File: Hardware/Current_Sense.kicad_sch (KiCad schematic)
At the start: 32 parts, among them IC2 INA241A4IDR, IC3 AMC1350DWVR, IC4 TLV9002QDRQ1, J6 Scrut Conn, SW3 Scrut Select, U9 REF35125QDBVR

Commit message: added models
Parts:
- added TP16: 1V25, TestPoint:TestPoint_Pad_1.0x1.0mm, symbol Connector:TestPoint
- R39: footprint WSBS8518L2500JKM4 -> Parts:WSBS8518L2500JKM4
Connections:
- net +1V25: now also TP16.1
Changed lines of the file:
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@@
 	(rectangle
 		(start 134.874 27.94)
-		(end 203.2 58.42)
+		(end 213.36 58.42)
 		(stroke
 			(width 0)
@@
 	(wire
 		(pts
+			(xy 201.93 45.72) (xy 201.93 46.99)
+		)
+		(stroke
+			(width 0)
+			(type default)
+		)
+	)
+	(wire
+		(pts
 			(xy 114.3 80.01) (xy 124.46 80.01)
 		)
@@
 			)
 		)
-		(property "Footprint" "WSBS8518L2500JKM4"
+		(property "Footprint" "Parts:WSBS8518L2500JKM4"
 			(at 21.59 136.83 0)
 			(effects
@@
 	)
 	(symbol
+		(lib_id "Connector:TestPoint")
+		(at 201.93 46.99 180)
+		(unit 1)
+		(exclude_from_sim no)
+		(in_bom no)
+		(on_board yes)
+		(dnp no)
+		(fields_autoplaced yes)
+		(property "Reference" "TP16"
+			(at 204.47 49.0219 0)
+			(effects
+				(font
+					(size 1.27 1.27)
+				)
+				(justify right)
+			)
+		)
+		(property "Value" "1V25"
+			(at 204.47 51.5619 0)
+			(effects
+				(font
+					(size 1.27 1.27)
+				)
+				(justify right)
+			)
+		)
+		(property "Footprint" "TestPoint:TestPoint_Pad_1.0x1.0mm"
+			(at 196.85 46.99 0)
+			(effects
+				(font
+					(size 1.27 1.27)
+				)
+				(hide yes)
+			)
+		)
+		(property "Datasheet" "~"
+			(at 196.85 46.99 0)
+			(effects
+				(font
+					(size 1.27 1.27)
+				)
+				(hide yes)
+			)
+		)
+		(property "Description" "test point"
+			(at 201.93 46.99 0)
+			(effects
+				(font
+					(size 1.27 1.27)
+				)
+				(hide yes)
+			)
+		)
+		(pin "1"
+		)
+		(instances
+			(project "PS-AmperesPCB"
+				(path "/a452d214-ea00-440d-a445-5d6103fda43a/7e38ba4d-a54c-4f69-a074-7d0a3dae713a"
+					(reference "TP16")
+					(unit 1)
+				)
+			)
+		)
+	)
+	(symbol
 		(lib_id "Device:R_Small")
 		(at 29.21 172.72 0)
@@
 					(unit 1)
 				)
+			)
+		)
+	)
+	(symbol
+		(lib_id "power:+1V35")
+		(at 201.93 45.72 0)
+		(unit 1)
+		(exclude_from_sim no)
+		(in_bom yes)
+		(on_board yes)
+		(dnp no)
+		(fields_autoplaced yes)
+		(property "Reference" "#PWR0127"
+			(at 201.93 49.53 0)
+			(effects
+				(font
+					(size 1.27 1.27)
+				)
+				(hide yes)
+			)
+		)
+		(property "Value" "+1V25"
+			(at 201.93 40.64 0)
+			(effects
+				(font
+					(size 1.27 1.27)
+				)
+			)
+		)
+		(property "Footprint" ""
+			(at 201.93 45.72 0)
+			(effects
+				(font
+					(size 1.27 1.27)
+				)
+				(hide yes)
+			)
+		)
+		(property "Datasheet" ""
+			(at 201.93 45.72 0)
+			(effects
+				(font
+					(size 1.27 1.27)
+				)
+				(hide yes)
+			)
+		)
+		(property "Description" "Power symbol creates a global label with name \"+1V35\""
+			(at 201.93 45.72 0)
+			(effects
+				(font
+					(size 1.27 1.27)
+				)
+				(hide yes)
+			)
+		)
+		(pin "1"
+		)
+		(instances
+			(project "PS-AmperesPCB"
+				(path "/a452d214-ea00-440d-a445-5d6103fda43a/7e38ba4d-a54c-4f69-a074-7d0a3dae713a"
+					(reference "#PWR0127")
+					(unit 1)
+				)

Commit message: updated some component part nums
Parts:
- C37, C40, C42, C45, C48, C49: Mfg (none) -> MLASH168SB7104KTNA01; P/N (none) -> MLASH168SB7104KTNA01
- C38, C41, C46, C47: Mfg (none) -> MLASU168SB5105KTNA01; P/N (none) -> MLASU168SB5105KTNA01
- C39: Mfg (none) -> GRM21BR61H106KE43K
- C43: Mfg (none) -> MLASU063SB7102KFNA01; P/N (none) -> MLASU063SB7102KFNA01
- R27: Mfg (none) -> CRCW06034K30FKEA; P/N (none) -> CRCW06034K30FKEA
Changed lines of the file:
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@@
 			)
 		)
+		(property "Mfg" "MLASU063SB7102KFNA01"
+			(at 114.3 82.55 0)
+			(effects
+				(font
+					(size 1.27 1.27)
+				)
+				(hide yes)
+			)
+		)
+		(property "P/N" "MLASU063SB7102KFNA01"
+			(at 114.3 82.55 0)
+			(effects
+				(font
+					(size 1.27 1.27)
+				)
+				(hide yes)
+			)
+		)
 		(pin "2"
 		)
@@
 			)
 		)
+		(property "Mfg" "MLASH168SB7104KTNA01"
+			(at 113.03 90.17 0)
+			(effects
+				(font
+					(size 1.27 1.27)
+				)
+				(hide yes)
+			)
+		)
+		(property "P/N" "MLASH168SB7104KTNA01"
+			(at 113.03 90.17 0)
+			(effects
+				(font
+					(size 1.27 1.27)
+				)
+				(hide yes)
+			)
+		)
 		(pin "2"
 		)
@@
 			)
 		)
+		(property "Mfg" "MLASH168SB7104KTNA01"
+			(at 162.56 90.17 0)
+			(effects
+				(font
+					(size 1.27 1.27)
+				)
+				(hide yes)
+			)
+		)
+		(property "P/N" "MLASH168SB7104KTNA01"
+			(at 162.56 90.17 0)
+			(effects
+				(font
+					(size 1.27 1.27)
+				)
+				(hide yes)
+			)
+		)
 		(pin "2"
 		)
@@
 			)
 		)
+		(property "Mfg" "MLASH168SB7104KTNA01"
+			(at 69.85 81.28 0)
+			(effects
+				(font
+					(size 1.27 1.27)
+				)
+				(hide yes)
+			)
+		)
+		(property "P/N" "MLASH168SB7104KTNA01"
+			(at 69.85 81.28 0)
+			(effects
+				(font
+					(size 1.27 1.27)
+				)
+				(hide yes)
+			)
+		)
 		(pin "2"
 		)
@@
 			)
 		)
+		(property "Mfg" "MLASH168SB7104KTNA01"
+			(at 144.78 48.26 0)
+			(effects
+				(font
+					(size 1.27 1.27)
+				)
+				(hide yes)
+			)
+		)
+		(property "P/N" "MLASH168SB7104KTNA01"
+			(at 144.78 48.26 0)
+			(effects
+				(font
+					(size 1.27 1.27)
+				)
+				(hide yes)
+			)
+		)
 		(pin "2"
 		)
@@
 			)
 		)
+		(property "Mfg" "CRCW06034K30FKEA"
+			(at 208.28 83.82 90)
+			(effects
+				(font
+					(size 1.27 1.27)
+				)
+				(hide yes)
+			)
+		)
+		(property "P/N" "CRCW06034K30FKEA"
+			(at 208.28 83.82 90)
+			(effects
+				(font
+					(size 1.27 1.27)
+				)
+				(hide yes)
+			)
+		)
 		(pin "2"
 		)
@@
 			)
 		)
+		(property "Mfg" "MLASU168SB5105KTNA01"
+			(at 121.92 90.17 0)
+			(effects
+				(font
+					(size 1.27 1.27)
+				)
+				(hide yes)
+			)
+		)
+		(property "P/N" "MLASU168SB5105KTNA01"
+			(at 121.92 90.17 0)
+			(effects
+				(font
+					(size 1.27 1.27)
+				)
+				(hide yes)
+			)
+		)
 		(pin "2"
 		)
@@
 			)
 		)
+		(property "Mfg" "GRM21BR61H106KE43K"
+			(at 175.26 49.53 0)
+			(effects
+				(font
+					(size 1.27 1.27)
+				)
+				(hide yes)
+			)
+		)
 		(pin "2"
 		)
@@
 			)
 		)
+		(property "Mfg" "MLASU168SB5105KTNA01"
+			(at 153.67 48.26 0)
+			(effects
+				(font
+					(size 1.27 1.27)
+				)
+				(hide yes)
+			)
+		)
+		(property "P/N" "MLASU168SB5105KTNA01"
+			(at 153.67 48.26 0)
+			(effects
+				(font
+					(size 1.27 1.27)
+				)
+				(hide yes)
+			)
+		)
 		(pin "2"
 		)
@@
 			)
 		)
+		(property "Mfg" "MLASU168SB5105KTNA01"
+			(at 212.09 74.93 0)
+			(effects
+				(font
+					(size 1.27 1.27)
+				)
+				(hide yes)
+			)
+		)
+		(property "P/N" "MLASU168SB5105KTNA01"
+			(at 212.09 74.93 0)
+			(effects
+				(font
+					(size 1.27 1.27)
+				)
+				(hide yes)
+			)
+		)
 		(pin "2"
 		)
@@
 			)
 		)
+		(property "Mfg" "MLASH168SB7104KTNA01"
+			(at 185.42 49.53 0)
+			(effects
+				(font
+					(size 1.27 1.27)
+				)
+				(hide yes)
+			)
+		)
+		(property "P/N" "MLASH168SB7104KTNA01"
+			(at 185.42 49.53 0)
+			(effects
+				(font
+					(size 1.27 1.27)
+				)
+				(hide yes)
+			)
+		)
 		(pin "2"
 		)
@@
 			)
 		)
+		(property "Mfg" "MLASH168SB7104KTNA01"
+			(at 251.46 105.41 0)
+			(effects
+				(font
+					(size 1.27 1.27)
+				)
+				(hide yes)
+			)
+		)
+		(property "P/N" "MLASH168SB7104KTNA01"
+			(at 251.46 105.41 0)
+			(effects
+				(font
+					(size 1.27 1.27)
+				)
+				(hide yes)
+			)
+		)
 		(pin "2"
 		)
@@
 			(at 154.94 90.17 0)
 			(effects
+				(font
+					(size 1.27 1.27)
+				)
+				(hide yes)
+			)
+		)
+		(property "Mfg" "MLASU168SB5105KTNA01"
+			(at 154.94 90.17 0)
+			(effects
+				(font
+					(size 1.27 1.27)
+				)
+				(hide yes)
+			)
+		)
+		(property "P/N" "MLASU168SB5105KTNA01"
+			(at 154.94 90.17 0)
+			(effects

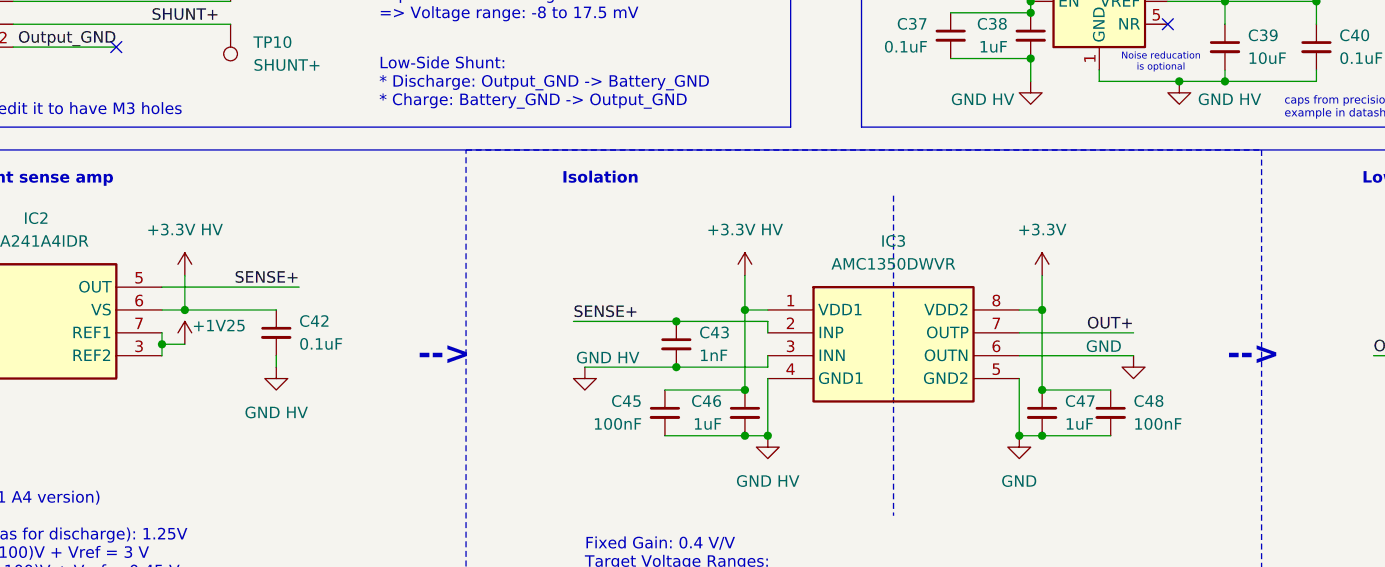
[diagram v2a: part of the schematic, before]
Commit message: new dpdt switch, layout done
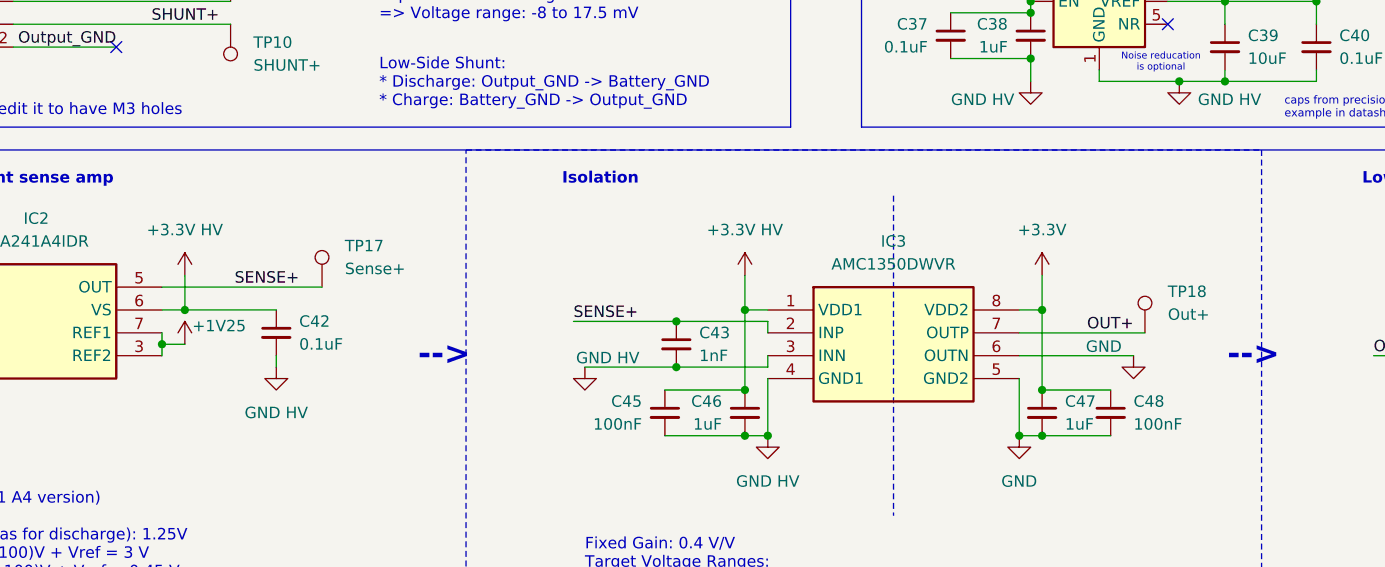
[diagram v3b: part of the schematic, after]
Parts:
- added TP17: Sense+, TestPoint:TestPoint_Keystone_5005-5009_Compact, symbol Connector:TestPoint
- added TP18: Out+, TestPoint:TestPoint_Keystone_5005-5009_Compact, symbol Connector:TestPoint
- J6: P/N (none) -> 105309-1202
- SW3: footprint Button_Switch_SMD:SW_DPDT_CK_JS202011JCQN -> Parts:CAS220TB
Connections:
- net OUT+: now also TP18.1
- net SENSE+: now also TP17.1
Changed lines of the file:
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@@
 	(wire
 		(pts
-			(xy 57.15 76.2) (xy 72.39 76.2)
+			(xy 57.15 76.2) (xy 74.93 76.2)
 		)
 		(stroke
@@
 	(wire
 		(pts
-			(xy 152.4 81.28) (xy 165.1 81.28)
+			(xy 152.4 81.28) (xy 166.37 81.28)
 		)
 		(stroke
@@
 	)
 	(symbol
+		(lib_id "Connector:TestPoint")
+		(at 166.37 81.28 0)
+		(unit 1)
+		(exclude_from_sim no)
+		(in_bom yes)
+		(on_board yes)
+		(dnp no)
+		(fields_autoplaced yes)
+		(property "Reference" "TP18"
+			(at 168.91 76.7079 0)
+			(effects
+				(font
+					(size 1.27 1.27)
+				)
+				(justify left)
+			)
+		)
+		(property "Value" "Out+"
+			(at 168.91 79.2479 0)
+			(effects
+				(font
+					(size 1.27 1.27)
+				)
+				(justify left)
+			)
+		)
+		(property "Footprint" "TestPoint:TestPoint_Keystone_5005-5009_Compact"
+			(at 171.45 81.28 0)
+			(effects
+				(font
+					(size 1.27 1.27)
+				)
+				(hide yes)
+			)
+		)
+		(property "Datasheet" "~"
+			(at 171.45 81.28 0)
+			(effects
+				(font
+					(size 1.27 1.27)
+				)
+				(hide yes)
+			)
+		)
+		(property "Description" "test point"
+			(at 166.37 81.28 0)
+			(effects
+				(font
+					(size 1.27 1.27)
+				)
+				(hide yes)
+			)
+		)
+		(pin "1"
+		)
+		(instances
+			(project ""
+				(path "/a452d214-ea00-440d-a445-5d6103fda43a/7e38ba4d-a54c-4f69-a074-7d0a3dae713a"
+					(reference "TP18")
+					(unit 1)
+				)
+			)
+		)
+	)
+	(symbol
 		(lib_id "Device:D_Zener")
 		(at 262.89 87.63 270)
@@
 			)
 		)
+		(property "P/N" "105309-1202"
+			(at 76.2 176.53 0)
+			(effects
+				(font
+					(size 1.27 1.27)
+				)
+				(hide yes)
+			)
+		)
 		(pin "2"
 		)
@@
 			)
 		)
-		(property "Footprint" "Button_Switch_SMD:SW_DPDT_CK_JS202011JCQN"
+		(property "Footprint" "Parts:CAS220TB"
 			(at 74.93 167.64 0)
 			(effects
@@
 			)
 		)
-		(property "Footprint" "Button_Switch_SMD:SW_DPDT_CK_JS202011JCQN"
+		(property "Footprint" "Parts:CAS220TB"
 			(at 74.93 152.4 0)
 			(effects
@@
 					(unit 1)
 				)
+			)
+		)
+	)
+	(symbol
+		(lib_id "Connector:TestPoint")
+		(at 74.93 76.2 0)
+		(unit 1)
+		(exclude_from_sim no)
+		(in_bom yes)
+		(on_board yes)
+		(dnp no)
+		(fields_autoplaced yes)
+		(property "Reference" "TP17"
+			(at 77.47 71.6279 0)
+			(effects
+				(font
+					(size 1.27 1.27)
+				)
+				(justify left)
+			)
+		)
+		(property "Value" "Sense+"
+			(at 77.47 74.1679 0)
+			(effects
+				(font
+					(size 1.27 1.27)
+				)
+				(justify left)
+			)
+		)
+		(property "Footprint" "TestPoint:TestPoint_Keystone_5005-5009_Compact"
+			(at 80.01 76.2 0)
+			(effects
+				(font
+					(size 1.27 1.27)
+				)
+				(hide yes)
+			)
+		)
+		(property "Datasheet" "~"
+			(at 80.01 76.2 0)
+			(effects
+				(font
+					(size 1.27 1.27)
+				)
+				(hide yes)
+			)
+		)
+		(property "Description" "test point"
+			(at 74.93 76.2 0)
+			(effects
+				(font
+					(size 1.27 1.27)
+				)
+				(hide yes)
+			)
+		)
+		(pin "1"
+		)
+		(instances
+			(project ""
+				(path "/a452d214-ea00-440d-a445-5d6103fda43a/7e38ba4d-a54c-4f69-a074-7d0a3dae713a"
+					(reference "TP17")
+					(unit 1)
+				)

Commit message: generated production stuff
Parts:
- IC2: P/N (none) -> INA241A4IDR
- IC3: P/N (none) -> AMC1350DWVR
- IC4: P/N (none) -> TLV9002QDRQ1
- R25: Mfg (none) -> 0603WAF8201T5E; P/N (none) -> 0603WAF8201T5E
- R26: Mfg (none) -> 0603WAJ0332T5E; P/N (none) -> 0603WAJ0332T5E
- R28: Mfg (none) -> 0603WAF3402T5E; P/N (none) -> 0603WAF3402T5E
- R29: Mfg (none) -> 0603WAF510JT5E; P/N (none) -> 0603WAF510JT5E
- R39: Manufacturer_Part_Number WSBS8518L2500JTP3 -> (none); Mfg (none) -> WSBS8518L2500JTP3; P/N (none) -> WSBS8518L2500JTP3
- SW3: Mfg (none) -> CAS-220TB; P/N (none) -> CAS-220TB
- U9: P/N (none) -> REF35125QDBVR
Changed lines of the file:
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@@
 			)
 		)
-		(property "Manufacturer_Part_Number" "WSBS8518L2500JTP3"
+		(property "P/N" "WSBS8518L2500JTP3"
 			(at 21.59 836.83 0)
 			(effects
@@
 			)
 		)
+		(property "Mfg" "WSBS8518L2500JTP3"
+			(at 40.64 41.91 0)
+			(effects
+				(font
+					(size 1.27 1.27)
+				)
+				(hide yes)
+			)
+		)
 		(pin "1"
 		)
@@
 			)
 		)
+		(property "Mfg" "0603WAF510JT5E"
+			(at 29.21 172.72 0)
+			(effects
+				(font
+					(size 1.27 1.27)
+				)
+				(hide yes)
+			)
+		)
+		(property "P/N" "0603WAF510JT5E"
+			(at 29.21 172.72 0)
+			(effects
+				(font
+					(size 1.27 1.27)
+				)
+				(hide yes)
+			)
+		)
 		(pin "1"
 		)
@@
 			)
 		)
+		(property "P/N" "INA241A4IDR"
+			(at 29.21 76.2 0)
+			(effects
+				(font
+					(size 1.27 1.27)
+				)
+				(hide yes)
+			)
+		)
 		(pin "8"
 		)
@@
 			)
 		)
+		(property "P/N" "TLV9002QDRQ1"
+			(at 218.44 81.28 0)
+			(effects
+				(font
+					(size 1.27 1.27)
+				)
+				(hide yes)
+			)
+		)
 		(pin "1"
 		)
@@
 			)
 		)
+		(property "P/N" "REF35125QDBVR"
+			(at 161.29 44.45 0)
+			(effects
+				(font
+					(size 1.27 1.27)
+				)
+				(hide yes)
+			)
+		)
 		(pin "2"
 		)
@@
 			)
 		)
+		(property "Mfg" "0603WAJ0332T5E"
+			(at 200.66 83.82 90)
+			(effects
+				(font
+					(size 1.27 1.27)
+				)
+				(hide yes)
+			)
+		)
+		(property "P/N" "0603WAJ0332T5E"
+			(at 200.66 83.82 90)
+			(effects
+				(font
+					(size 1.27 1.27)
+				)
+				(hide yes)
+			)
+		)
 		(pin "2"
 		)
@@
 			)
 		)
+		(property "Mfg" "0603WAF3402T5E"
+			(at 29.21 160.02 0)
+			(effects
+				(font
+					(size 1.27 1.27)
+				)
+				(hide yes)
+			)
+		)
+		(property "P/N" "0603WAF3402T5E"
+			(at 29.21 160.02 0)
+			(effects
+				(font
+					(size 1.27 1.27)
+				)
+				(hide yes)
+			)
+		)
 		(pin "1"
 		)
@@
 			)
 		)
-		(property "Datasheet" "~"
+		(property "Datasheet" "https://www.nidec-components.com/e/catalog/switch/cas.pdf"
 			(at 74.93 167.64 0)
 			(effects
@@
 			)
 		)
+		(property "P/N" "CAS-220TB"
+			(at 74.93 167.64 0)
+			(effects
+				(font
+					(size 1.27 1.27)
+				)
+				(hide yes)
+			)
+		)
+		(property "Mfg" "CAS-220TB"
+			(at 74.93 167.64 0)
+			(effects
+				(font
+					(size 1.27 1.27)
+				)
+				(hide yes)
+			)
+		)
 		(pin "5"
 		)
@@
 			)
 		)
+		(property "P/N" "AMC1350DWVR"
+			(at 124.46 78.74 0)
+			(effects
+				(font
+					(size 1.27 1.27)
+				)
+				(hide yes)
+			)
+		)
 		(pin "6"
 		)
@@
 			)
 		)
-		(property "Datasheet" "~"
+		(property "Datasheet" "https://www.nidec-components.com/e/catalog/switch/cas.pdf"
 			(at 74.93 152.4 0)
 			(effects
@@
 			)
 		)
+		(property "P/N" "CAS-220TB"
+			(at 74.93 152.4 0)
+			(effects
+				(font
+					(size 1.27 1.27)
+				)
+				(hide yes)
+			)
+		)
+		(property "Mfg" "CAS-220TB"
+			(at 74.93 152.4 0)
+			(effects
+				(font
+					(size 1.27 1.27)
+				)
+				(hide yes)
+			)
+		)
 		(pin "5"
 		)
@@
 			(at 204.47 74.93 0)
 			(effects
+				(font
+					(size 1.27 1.27)
+				)
+				(hide yes)
+			)
+		)
+		(property "Mfg" "0603WAF8201T5E"
+			(at 204.47 74.93 0)
+			(effects
+				(font
+					(size 1.27 1.27)
+				)
+				(hide yes)
+			)
+		)
+		(property "P/N" "0603WAF8201T5E"
+			(at 204.47 74.93 0)
+			(effects

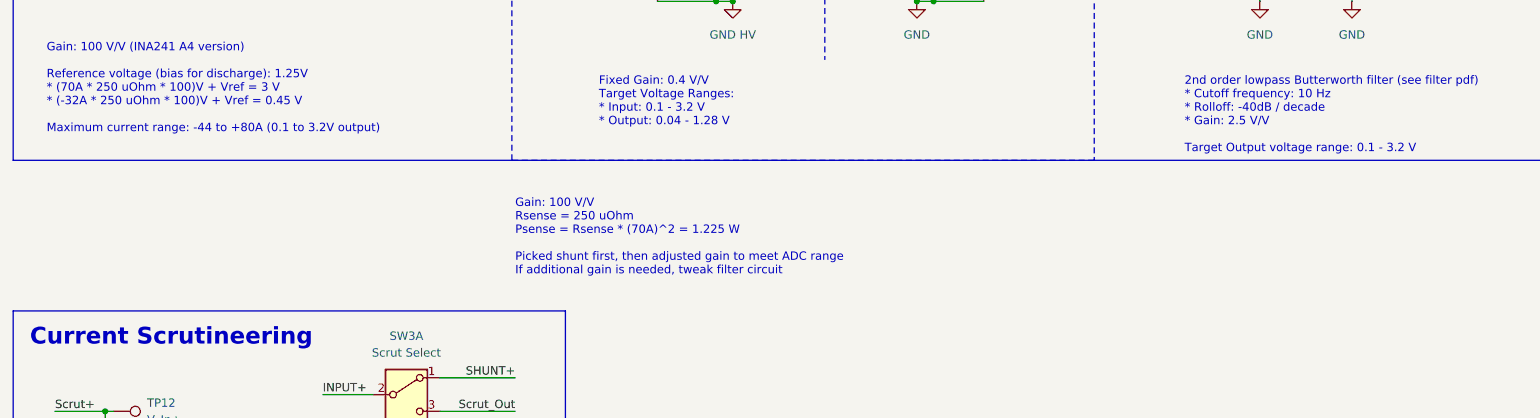
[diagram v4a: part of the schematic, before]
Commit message: updated amperes docs
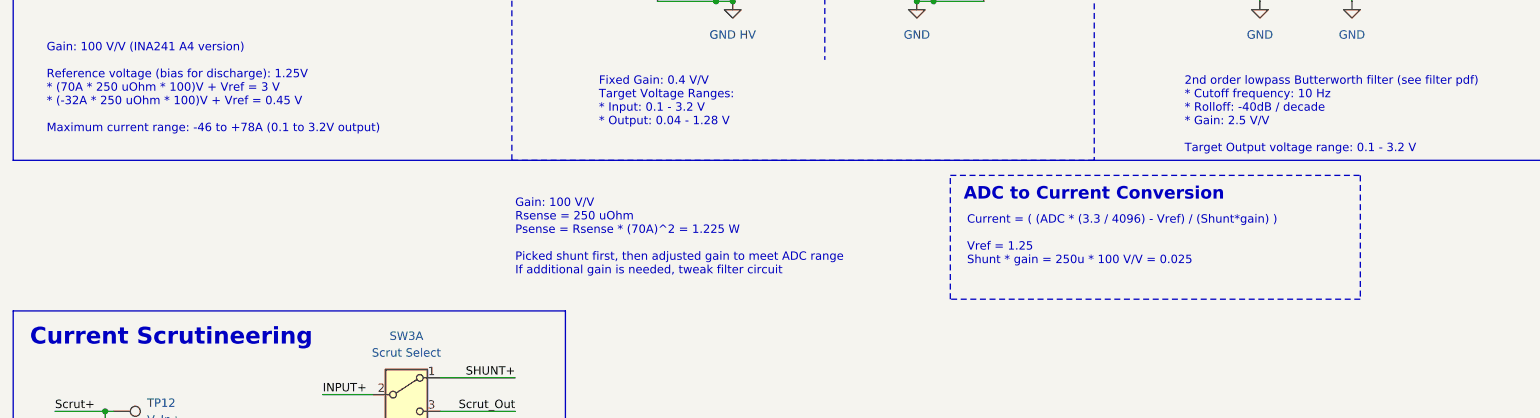
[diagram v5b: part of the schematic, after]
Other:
- note added: "ADC to Current Conversion"
- note added: "Current = ( (ADC * (3.3 / 4096) - Vref) / (Shunt*gain) ) Vref = 1.25 Shunt * gain = 250u * 100 V/V = 0.025"
- note added: "Gain: 100 V/V (INA241 A4 version) Reference voltage (bias for discharge): 1.25V * (70A * 250 uOhm * 100)V + Vref = 3 V * (-32A * 250 uOhm * 100)V + Vref = 0.45 V Maximum current range: -46 to +78A (0.1 to 3.2V output)"
- note removed: "Gain: 100 V/V (INA241 A4 version) Reference voltage (bias for discharge): 1.25V * (70A * 250 uOhm * 100)V + Vref = 3 V * (-32A * 250 uOhm * 100)V + Vref = 0.45 V Maximum current range: -44 to +80A (0.1 to 3.2V output)"
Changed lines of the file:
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@@
 	(paper "A4")
+	(rectangle
+		(start 157.48 119.126)
+		(end 219.71 137.922)
+		(stroke
+			(width 0)
+			(type dash)
+		)
+		(fill
+			(type none)
+		)
+	)
 	(rectangle
 		(start 15.24 27.94)
@@
 		)
 	)
-	(text "Gain: 100 V/V (INA241 A4 version)\n\nReference voltage (bias for discharge): 1.25V\n* (70A * 250 uOhm * 100)V + Vref = 3 V\n* (-32A * 250 uOhm * 100)V + Vref = 0.45 V\n\nMaximum current range: -44 to +80A (0.1 to 3.2V output)"
+	(text "Gain: 100 V/V (INA241 A4 version)\n\nReference voltage (bias for discharge): 1.25V\n* (70A * 250 uOhm * 100)V + Vref = 3 V\n* (-32A * 250 uOhm * 100)V + Vref = 0.45 V\n\nMaximum current range: -46 to +78A (0.1 to 3.2V output)"
 		(exclude_from_sim no)
 		(at 20.32 99.06 0)
@@
 		)
 	)
+	(text "Current = ( (ADC * (3.3 / 4096) - Vref) / (Shunt*gain) )\n\nVref = 1.25\nShunt * gain = 250u * 100 V/V = 0.025\n"
+		(exclude_from_sim no)
+		(at 160.02 125.222 0)
+		(effects
+			(font
+				(size 1.27 1.27)
+			)
+			(justify left top)
+		)
+	)
 	(text "Gain: 100 V/V\nRsense = 250 uOhm\nPsense = Rsense * (70A)^2 = 1.225 W\n\nPicked shunt first, then adjusted gain to meet ADC range\nIf additional gain is needed, tweak filter circuit"
 		(exclude_from_sim no)
@@
 			)
 			(justify left top)
+		)
+	)
+	(text "ADC to Current Conversion"
+		(exclude_from_sim no)
+		(at 159.512 120.904 0)
+		(effects
+			(font
+				(size 1.905 1.905)
+				(thickness 0.508)
+				(bold yes)
+			)
+			(justify left top)
